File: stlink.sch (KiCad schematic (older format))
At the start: 36 parts, among them Con4 USB_C_Wurth_632723130112, Q1 BC847B, U5 STM32F103C(8-B)Tx, U6 MCP1700T-3302E_MB, X1 8.000MHZ

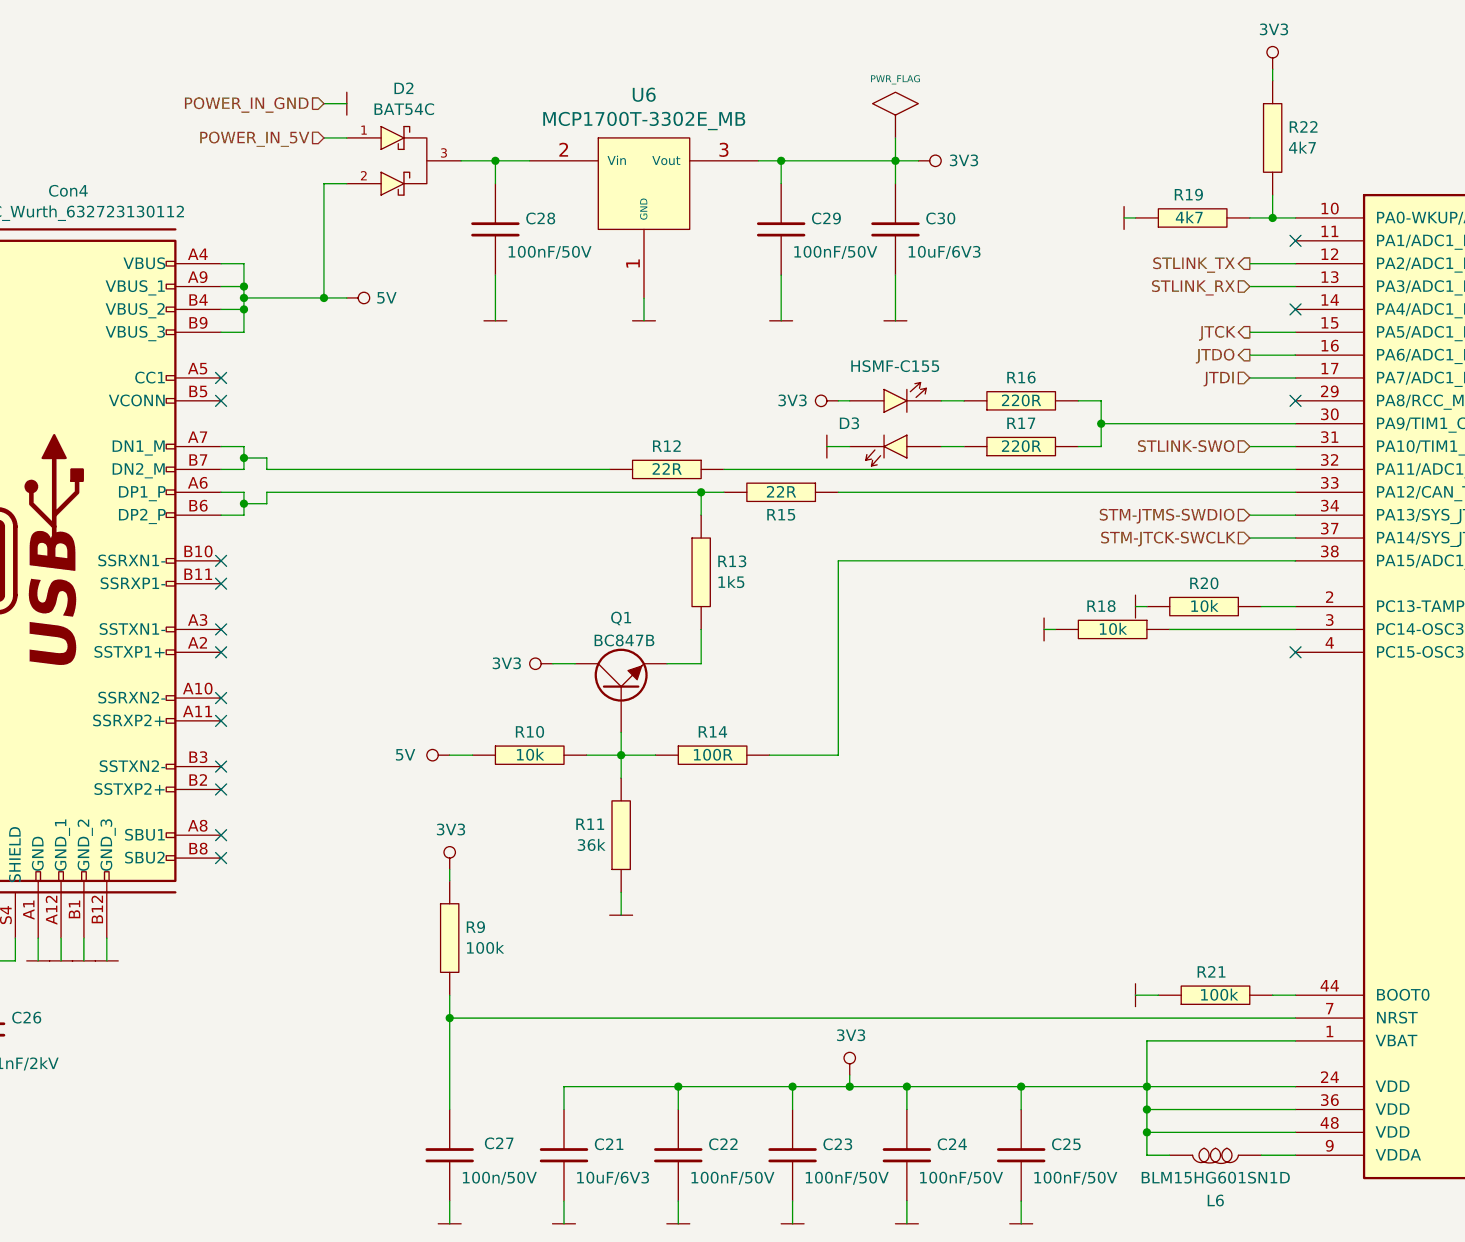
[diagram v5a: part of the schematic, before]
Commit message: Tracking finished, started tunning
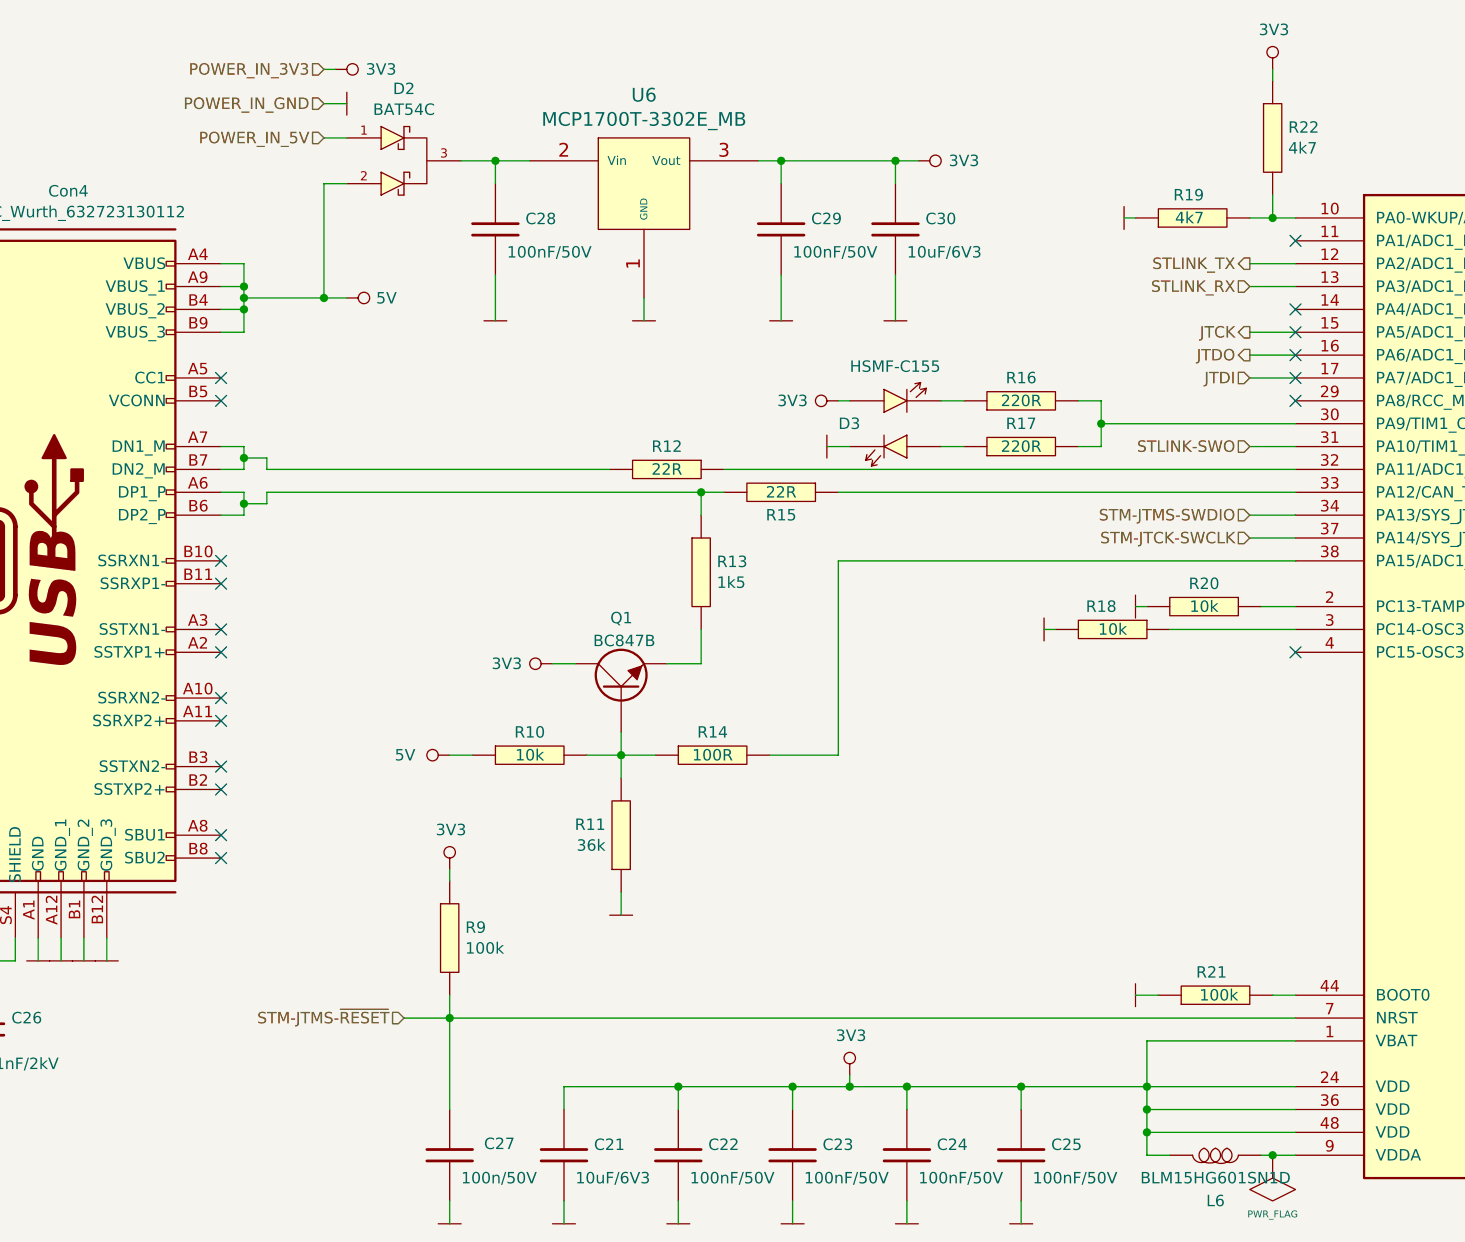
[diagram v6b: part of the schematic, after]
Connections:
- net STM-JTMS-~RESET~: now reaches C27.1, R9.2, U5.7 (NRST)
- no-connect marks 26 -> 29
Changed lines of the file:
@@
 $Descr A3 16535 11693
 encoding utf-8
-Sheet 9 11
+Sheet 11 11
 Title "STLink Module"
 Date "2020-12-20"
@@
 $EndComp
 Wire Wire Line
-	7200 7600 7050 7600
+	7200 7600 7100 7600
 Wire Wire Line
 	7200 7500 6550 7500
@@
 $EndComp
 Wire Wire Line
-	3700 3950 3700 3750
-Wire Wire Line
 	3700 3350 3700 3250
 Connection ~ 3700 3250
@@
 	5550 3250 5450 3250
 Connection ~ 5450 3250
-$Comp
-L power:PWR_FLAG #FLG0103
-U 1 1 60338A79
-P 5450 3150
-F 0 "#FLG0103" H 5450 3420 30  0001 C CNN
-F 1 "PWR_FLAG" H 5450 3408 30  0000 C CNN
-F 2 "" H 5450 3150 60  0000 C CNN
-F 3 "" H 5450 3150 60  0000 C CNN
-	1    5450 3150
-	1    0    0    -1
-$EndComp
-Wire Wire Line
-	5450 3150 5450 3250
 Text HLabel 15000 4500 2    50   Input ~ 0
 JTMS
@@
 Wire Wire Line
 	1450 6750 1500 6750
+NoConn ~ 7200 4000
+NoConn ~ 7200 4100
+NoConn ~ 7200 4200
+$Comp
+L power:PWR_FLAG #FLG0111
+U 1 1 6016CC38
+P 7100 7600
+F 0 "#FLG0111" H 7100 7870 30  0001 C CNN
+F 1 "PWR_FLAG" H 7100 7858 30  0000 C CNN
+F 2 "" H 7100 7600 60  0000 C CNN
+F 3 "" H 7100 7600 60  0000 C CNN
+	1    7100 7600
+	-1   0    0    1
+$EndComp
+Connection ~ 7100 7600
+Wire Wire Line
+	7100 7600 7050 7600
+$Comp
+L power:3V3_NO_GLOBAL #PWR198
+U 1 1 60176FED
+P 3000 2850
+F 0 "#PWR198" H 3000 2950 40  0001 C CNN
+F 1 "3V3" V 3000 3050 50  0000 C CNN
+F 2 "" H 3000 2850 60  0000 C CNN
+F 3 "" H 3000 2850 60  0000 C CNN
+	1    3000 2850
+	0    1    1    0
+$EndComp
+Text HLabel 2950 2850 0    50   Input ~ 0
+POWER_IN_3V3
+Wire Wire Line
+	2950 2850 3000 2850
+Wire Wire Line
+	3700 3750 3700 3950
+Text HLabel 3300 7000 0    50   Input ~ 0
+STM-JTMS-~RESET~
+Wire Wire Line
+	3500 7000 3300 7000
 $EndSCHEMATC
